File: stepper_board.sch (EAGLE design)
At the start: 71 parts, among them IC1 MCP1703DB, U2 MIC2005A-1YM5, Y1 12 MHz

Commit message: Routed tons o' stuff
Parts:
- removed D4: ES2D, diode:ES2D
- added D5: PD3S160, diode:PD3S160
- added SV10: (no value), con-lstb:MA05-1
- SV9: device con-lstb:MA05-1 -> con-lstb:MA04-1
- renumbered LED1 to PWR
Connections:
- removed net GPIO3: STM32F411RE.PA15/JTDI, SV9.2
- removed net GPIO4: STM32F411RE.PA8, SV9.3
- removed net OSCIN1: DRV1.OSCIN
- removed net OSCIN2: DRV2.OSCIN
- removed net OSCIN3: DRV3.OSCIN
- removed net OSCOUT1: DRV1.OSCOUT
- removed net OSCOUT2: DRV2.OSCOUT
- removed net OSCOUT3: DRV3.OSCOUT
- new net GPIO1: STM32F411RE.PA14/JTCK, SV9.3
- new net SPI2_MISO: SV10.3
- new net USB_EN: STM32F411RE.PA8, U2.EN
- net +3V3: now also STM32F411RE.VBAT, SV10.2, SV9.2; no longer SV9.4
- net GND: now also DRV1.ADCIN, DRV2.ADCIN, DRV3.ADCIN, SV10.1, SV9.1; no longer SV9.5
- net GPIO2: now also STM32F411RE.PA15/JTDI, SV9.4; no longer STM32F411RE.PA14/JTCK, SV9.1
- net SPI2_MOSI: now also SV10.4
- net SPI2_SCK: now also SV10.5
- net USB_VBUS: now also D5.A; no longer D4.A
- net V+: now also D5.C; no longer D4.C
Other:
- note added: "SPI Header"
- moved on the sheet: C1, C10, C11, C13, C2, C20, C21, C5, C6, C9, DRV1, DRV3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

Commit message: Finished routing! Also added test points.
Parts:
- added TP1, TP2, TP3, TP4: PTR1B1,27, testpad:PTR1B1,27
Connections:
- removed net GPIO2: STM32F411RE.PA15/JTDI, SV9.4
- net +3V3: now also TP3.TP
- net ADC0: now also STM32F411RE.PA0
- net ADC1_14: now also TP2.TP
- net ADC1_15: now also TP1.TP
- net ADC6: now also STM32F411RE.PA6/SPI1_MISO
- net CS1: now also STM32F411RE.PB0
- net CS3: now also STM32F411RE.PA15/JTDI
- net GND: now also SV9.4, TP4.TP
- net SPI2_MISO: now also STM32F411RE.PC2

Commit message: Added reset switch, thermal pad vias, cleaned up some traces, and fixed usb footprint
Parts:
- added C31: 100n, rcl:C-USC0805
- added R6: 4k7, rcl:R-US_R0805
- added S1: (no value), switch-omron:10-XX
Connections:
- net +3V3: now also R6.2
- net GND: now also C31.2, S1.P1
- net RESET: now also C31.1, R6.1, S1.S
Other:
- note added: "Reset Switch"
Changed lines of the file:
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@@
 <part name="TP3" library="testpad" deviceset="PTR1" device="B1,27"/>
 <part name="TP4" library="testpad" deviceset="PTR1" device="B1,27"/>
+<part name="S1" library="switch-omron" deviceset="10-XX" device=""/>
+<part name="C31" library="rcl" deviceset="C-US" device="C0805" value="100n"/>
+<part name="GND19" library="supply1" deviceset="GND" device=""/>
+<part name="+3V10" library="supply1" deviceset="+3V3" device=""/>
+<part name="R6" library="rcl" deviceset="R-US_" device="R0805" value="4k7"/>
 </parts>
 <sheets>
@@
 <text x="134.62" y="-20.32" size="1.778" layer="91">GPIO Header</text>
 <text x="134.62" y="10.16" size="1.778" layer="91">SPI Header</text>
+<text x="129.54" y="-50.8" size="1.778" layer="91">Reset Switch</text>
 </plain>
 <instances>
@@
 <instance part="TP3" gate="G$1" x="-43.18" y="-58.42"/>
 <instance part="TP4" gate="G$1" x="-48.26" y="-88.9"/>
+<instance part="S1" gate="1" x="129.54" y="-78.74"/>
+<instance part="C31" gate="G$1" x="139.7" y="-76.2"/>
+<instance part="GND19" gate="1" x="132.08" y="-91.44"/>
+<instance part="+3V10" gate="G$1" x="129.54" y="-53.34"/>
+<instance part="R6" gate="G$1" x="129.54" y="-63.5" rot="R90"/>
 </instances>
 <busses>
@@
 <pinref part="SV9" gate="1" pin="4"/>
 </segment>
+<segment>
+<pinref part="GND19" gate="1" pin="GND"/>
+<pinref part="S1" gate="1" pin="P1"/>
+<wire x1="132.08" y1="-83.82" x2="132.08" y2="-86.36" width="0.1524" layer="91"/>
+<pinref part="C31" gate="G$1" pin="2"/>
+<wire x1="132.08" y1="-86.36" x2="132.08" y2="-88.9" width="0.1524" layer="91"/>
+<wire x1="139.7" y1="-81.28" x2="139.7" y2="-86.36" width="0.1524" layer="91"/>
+<wire x1="139.7" y1="-86.36" x2="132.08" y2="-86.36" width="0.1524" layer="91"/>
+<junction x="132.08" y="-86.36"/>
+</segment>
 </net>
 <net name="1_OUT1A" class="0">
@@
 <wire x1="139.7" y1="2.54" x2="137.16" y2="2.54" width="0.1524" layer="91"/>
 <label x="137.16" y="2.54" size="1.27" layer="95" rot="R180" xref="yes"/>
+</segment>
+<segment>
+<pinref part="R6" gate="G$1" pin="2"/>
+<pinref part="+3V10" gate="G$1" pin="+3V3"/>
+<wire x1="129.54" y1="-58.42" x2="129.54" y2="-55.88" width="0.1524" layer="91"/>
 </segment>
 </net>
@@
 <label x="-30.48" y="25.4" size="1.27" layer="95" rot="R180" xref="yes"/>
 </segment>
-</net>
+<segment>
+<pinref part="S1" gate="1" pin="S"/>
+<pinref part="R6" gate="G$1" pin="1"/>
+<wire x1="129.54" y1="-68.58" x2="129.54" y2="-71.12" width="0.1524" layer="91"/>
+<pinref part="C31" gate="G$1" pin="1"/>
+<wire x1="129.54" y1="-71.12" x2="129.54" y2="-73.66" width="0.1524" layer="91"/>
+<wire x1="139.7" y1="-73.66" x2="139.7" y2="-71.12" width="0.1524" layer="91"/>
+<wire x1="139.7" y1="-71.12" x2="129.54" y2="-71.12" width="0.1524" layer="91"/>
+<junction x="129.54" y="-71.12"/>
+<wire x1="139.7" y1="-71.12" x2="149.86" y2="-71.12" width="0.1524" layer="91"/>
+<junction x="139.7" y="-71.12"/>
+<label x="149.86" y="-71.12" size="1.27" layer="95" xref="yes"/>
+</segment>
+</net>

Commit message: Modified silkscreen layer to make labels clear
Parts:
- renumbered IC1 to VREG, OUTA1 to OA1, OUTA2 to OA2, OUTA3 to OA3, OUTB1 to OB1, OUTB2 to OB2, OUTB3 to OB3, S1 to RST, SD1 to MICROSD, STM32F411RE to MCU, SV1 to ADC, SV10 to SPI, SV2 to 3V3, SV3 to GND, SV4 to JSTK, SV5 to RTC, SV6 to I2C, SV7 to UART, SV8 to BOOTJMP, SV9 to GPIO, U$1 to ESD, U1 to USB, U2 to CUR, Y1 to OSC

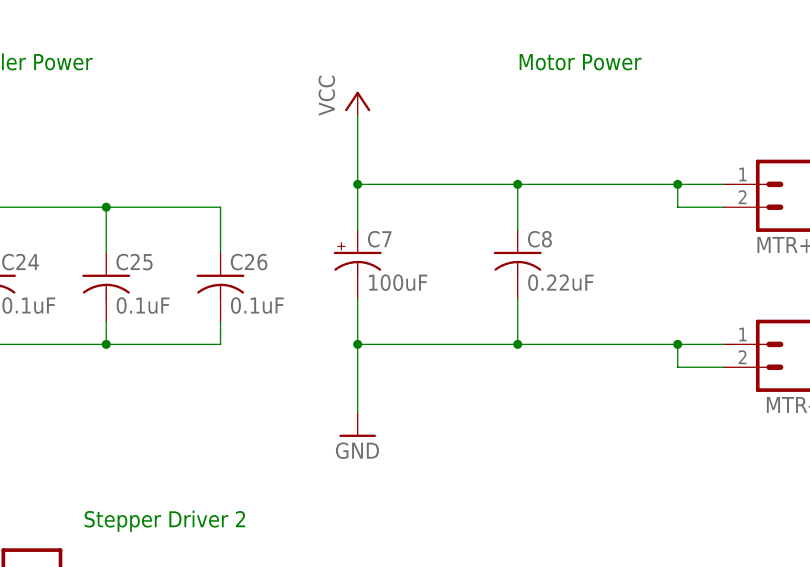
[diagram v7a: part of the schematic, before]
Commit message: Changed value of motor blocking cap
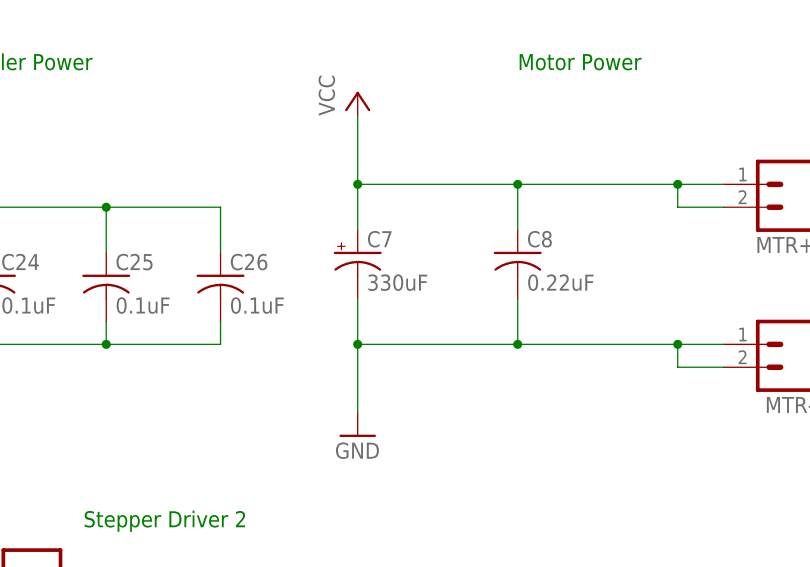
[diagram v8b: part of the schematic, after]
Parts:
- C7: value 100uF -> 330uF
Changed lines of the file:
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@@
 <?xml version="1.0" encoding="utf-8"?>
 <!DOCTYPE eagle SYSTEM "eagle.dtd">
-<eagle version="7.7.0">
+<eagle version="6.6.0">
 <drawing>
 <settings>
@@
 <part name="MTR-" library="con-amp-quick" deviceset="M02" device=""/>
 <part name="VCC3" library="supply1" deviceset="VCC" device=""/>
-<part name="C7" library="rcl" deviceset="CPOL-US" device="UD-10X10" value="100uF"/>
+<part name="C7" library="rcl" deviceset="CPOL-US" device="UD-10X10" value="330uF"/>
 <part name="C8" library="rcl" deviceset="C-US" device="C0805" value="0.22uF"/>
 <part name="GND4" library="supply1" deviceset="GND" device=""/>
